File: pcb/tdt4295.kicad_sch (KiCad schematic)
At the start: 1 part, among them U2 TPS54325PWP

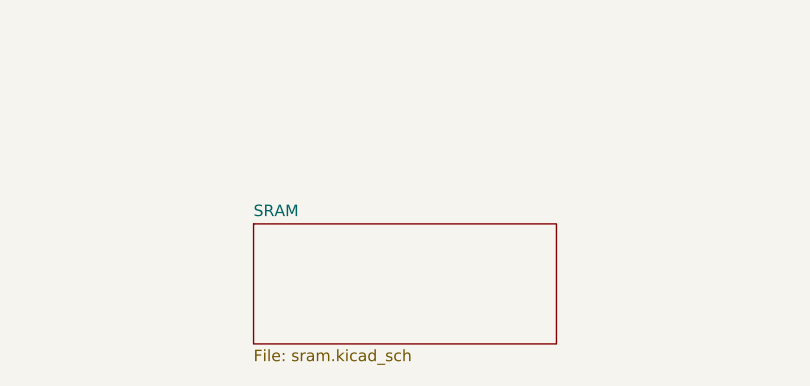
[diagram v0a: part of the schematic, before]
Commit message: shield -> ground
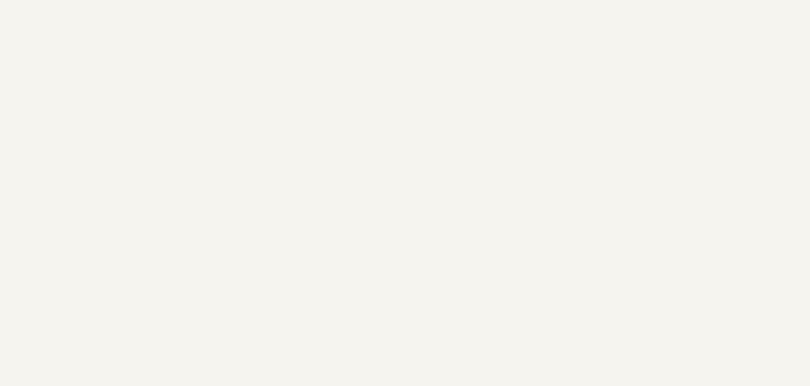
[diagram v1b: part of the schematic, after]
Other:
- removed sheet SRAM
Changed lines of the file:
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@@
-	)
-	(sheet
-		(at 114.3 95.25)
-		(size 33.655 13.335)
-		(exclude_from_sim no)
-		(in_bom yes)
-		(on_board yes)
-		(dnp no)
-		(fields_autoplaced yes)
-		(stroke
-			(width 0.1524)
-			(type solid)
-		)
-		(fill
-			(color 0 0 0 0)
-		)
-		(property "Sheetname" "SRAM"
-			(at 114.3 94.5384 0)
-			(show_name no)
-			(do_not_autoplace no)
-			(effects
-				(font
-					(size 1.27 1.27)
-				)
-				(justify left bottom)
-			)
-		)
-		(property "Sheetfile" "sram.kicad_sch"
-			(at 114.3 109.1696 0)
-			(show_name no)
-			(do_not_autoplace no)
-			(effects
-				(font
-					(size 1.27 1.27)
-				)
-				(justify left top)
-			)
-		)
-		(instances
-			(project "tdt4295"
-				(path "/603dd496-f9c4-4a31-9104-19eec41ebc98"
-					(page "11")
-				)
-			)
-		)
 	)
 	(sheet

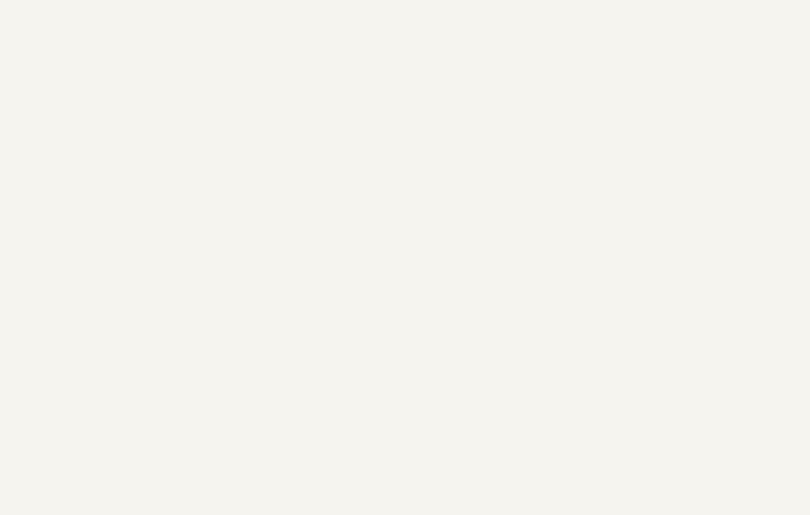
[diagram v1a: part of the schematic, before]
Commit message: pcb: add fpga to root
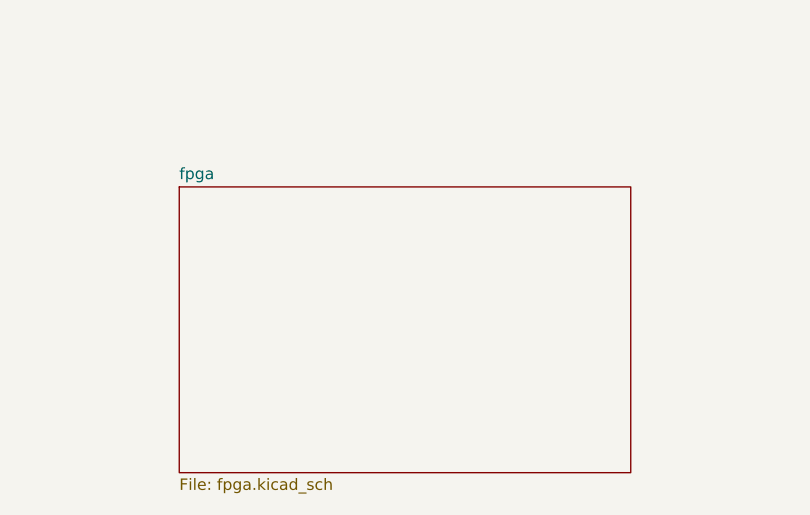
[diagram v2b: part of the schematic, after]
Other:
- added sheet fpga (fpga.kicad_sch)
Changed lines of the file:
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@@
+	)
+	(sheet
+		(at 111.76 83.82)
+		(size 50.165 31.75)
+		(exclude_from_sim no)
+		(in_bom yes)
+		(on_board yes)
+		(dnp no)
+		(fields_autoplaced yes)
+		(stroke
+			(width 0.1524)
+			(type solid)
+		)
+		(fill
+			(color 0 0 0 0)
+		)
+		(property "Sheetname" "fpga"
+			(at 111.76 83.1084 0)
+			(show_name no)
+			(do_not_autoplace no)
+			(effects
+				(font
+					(size 1.27 1.27)
+				)
+				(justify left bottom)
+			)
+		)
+		(property "Sheetfile" "fpga.kicad_sch"
+			(at 111.76 116.1546 0)
+			(show_name no)
+			(do_not_autoplace no)
+			(effects
+				(font
+					(size 1.27 1.27)
+				)
+				(justify left top)
+			)
+		)
+		(instances
+			(project "tdt4295"
+				(path "/603dd496-f9c4-4a31-9104-19eec41ebc98"
+					(page "2")
+				)
+			)
+		)
 	)
 	(sheet

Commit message: fpga connection and cleanup
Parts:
- removed U2: TPS54325PWP, PWP14_2P31X2P46, symbol TPS54325:TPS54325PWP
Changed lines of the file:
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@@
 	(generator_version "10.0")
 	(paper "A4")
-	(symbol
-		(lib_id "TPS54325:TPS54325PWP")
-		(at 193.04 67.31 0)
-		(unit 1)
-		(body_style 1)
-		(exclude_from_sim no)
-		(in_bom yes)
-		(on_board yes)
-		(in_pos_files yes)
-		(dnp no)
-		(fields_autoplaced yes)
-		(property "Reference" "U2"
-			(at 240.03 74.93 0)
-			(show_name no)
-			(do_not_autoplace no)
-			(effects
-				(font
-					(size 1.524 1.524)
-				)
-			)
-		)
-		(property "Value" "TPS54325PWP"
-			(at 240.03 77.47 0)
-			(show_name no)
-			(do_not_autoplace no)
-			(effects
-				(font
-					(size 1.524 1.524)
-				)
-			)
-		)
-		(property "Footprint" "PWP14_2P31X2P46"
-			(at 207.01 85.09 0)
-			(hide yes)
-			(show_name no)
-			(do_not_autoplace no)
-			(effects
-				(font
-					(size 1.27 1.27)
-					(italic yes)
-				)
-			)
-		)
-		(property "Datasheet" "https://www.ti.com/lit/gpn/tps54325"
-			(at 193.04 67.31 0)
-			(hide yes)
-			(show_name no)
-			(do_not_autoplace no)
-			(effects
-				(font
-					(size 1.27 1.27)
-					(italic yes)
-				)
-			)
-		)
-		(property "Description" ""
-			(at 193.04 67.31 0)
-			(hide yes)
-			(show_name no)
-			(do_not_autoplace no)
-			(effects
-				(font
-					(size 1.27 1.27)
-				)
-			)
-		)
-		(pin "9"
-		)
-		(pin "3"
-		)
-		(pin "5"
-		)
-		(pin "4"
-		)
-		(pin "14"
-		)
-		(pin "10"
-		)
-		(pin "15"
-		)
-		(pin "12"
-		)
-		(pin "6"
-		)
-		(pin "13"
-		)
-		(pin "8"
-		)
-		(pin "1"
-		)
-		(pin "2"
-		)
-		(pin "11"
-		)
-		(pin "7"
-		)
-		(instances
-			(project "tdt4295"
-				(path "/603dd496-f9c4-4a31-9104-19eec41ebc98"
-					(reference "U2")
-					(unit 1)
-				)
-			)
-		)
-	)
 	(sheet
 		(at 54.61 38.1)
